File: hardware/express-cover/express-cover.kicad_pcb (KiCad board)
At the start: 2 copper layers, 180 x 35 mm, 26 parts

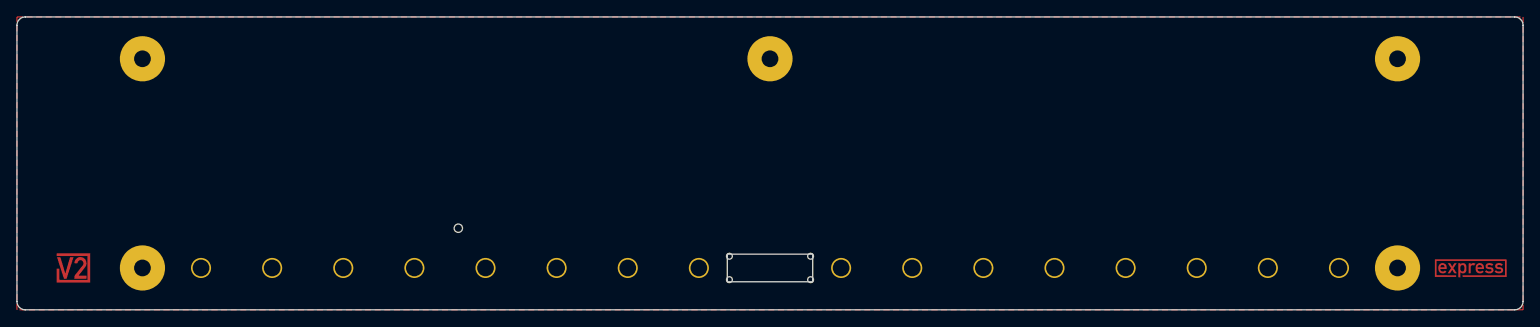
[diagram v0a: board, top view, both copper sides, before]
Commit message: Replace Order_Number
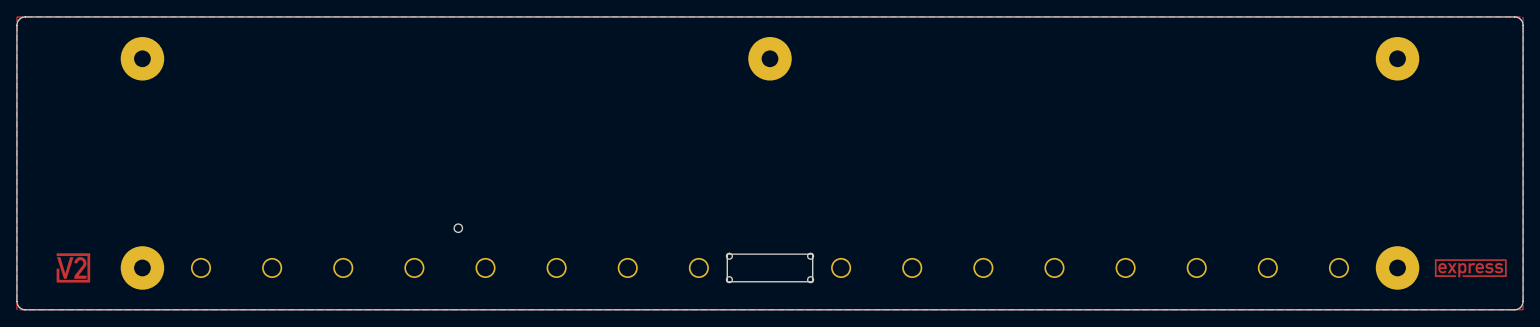
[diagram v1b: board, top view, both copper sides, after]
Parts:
- H101, H104, H107, H110, H113: value MountingHole_2mm_Pad_5.2mm -> 2mm_Pad_5.2mm
- H102, H103, H105, H106, H108, H109, H111, H112, H114, H115, H116, H117, H118, H119, H120, H121: value MountingHole_2mm_Pad_2.4mm -> 2mm_Pad_2.4mm
- H122: value MountingHole_1mm -> 1mm
- INFO101: value Order_Number -> ~; footprint V2_Production:Order_Number -> V2_Production:Revision
